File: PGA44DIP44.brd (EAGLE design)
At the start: 58.4 x 20.3 mm, 6 parts

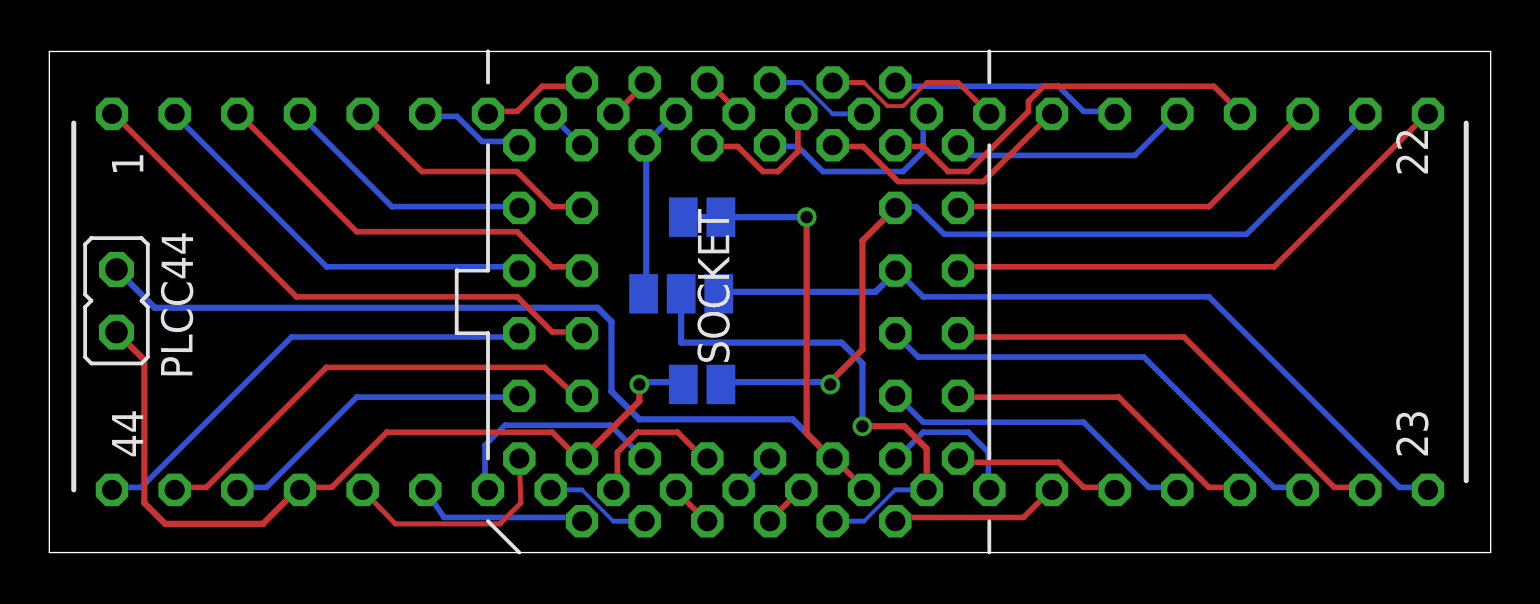
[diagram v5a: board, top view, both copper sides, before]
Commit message: * Fatal misassignment fixed for PGA44. * Update to EAGLE 8.1.0
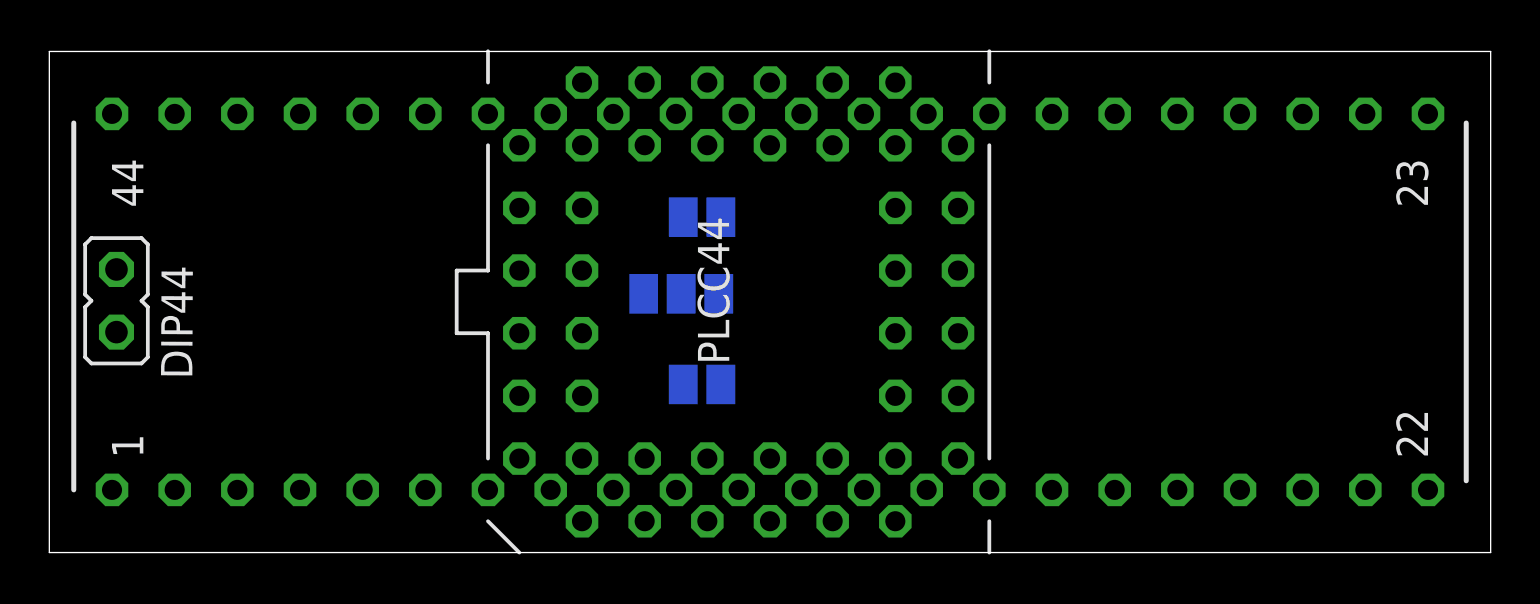
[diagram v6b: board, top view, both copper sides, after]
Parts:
- removed SOCKET: (no value), PGA44DIP44:PGA44
- added DIP44: DIP44, PGA44DIP44:DIP44
- PLCC44: value DIP44 -> PGA44; device PGA44DIP44:DIP44 -> PGA44DIP44:PGA44
- moved PLCC44 1.80 mm to (27.9, 10.2), turned to 90 degrees
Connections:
- net L1: now also DIP44.1; no longer SOCKET.1
- net L10: now also DIP44.10; no longer SOCKET.10
- net L11: now also DIP44.11; no longer SOCKET.11
- net L12: now also DIP44.12; no longer SOCKET.12
- net L13: now also DIP44.13; no longer SOCKET.13
- net L14: now also DIP44.14; no longer SOCKET.14
- net L15: now also DIP44.15; no longer SOCKET.15
- net L16: now also DIP44.16; no longer SOCKET.16
- net L17: now also DIP44.17; no longer SOCKET.17
- net L18: now also DIP44.18; no longer SOCKET.18
- net L19: now also DIP44.19; no longer SOCKET.19
- net L2: now also DIP44.2; no longer SOCKET.2
- net L20: now also DIP44.20; no longer SOCKET.20
- net L21: now also DIP44.21; no longer SOCKET.21
- net L22: now also DIP44.22; no longer SOCKET.22
- net L23: now also DIP44.23; no longer SOCKET.23
- net L24: now also DIP44.24; no longer SOCKET.24
- net L25: now also DIP44.25; no longer SOCKET.25
- net L26: now also DIP44.26; no longer SOCKET.26
- net L27: now also DIP44.27; no longer SOCKET.27
- net L28: now also DIP44.28; no longer SOCKET.28
- net L29: now also DIP44.29; no longer SOCKET.29
- net L3: now also DIP44.3; no longer SOCKET.3
- net L30: now also DIP44.30; no longer SOCKET.30
- net L31: now also DIP44.31; no longer SOCKET.31
- net L32: now also DIP44.32; no longer SOCKET.32
- net L33: now also DIP44.33; no longer SOCKET.33
- net L34: now also DIP44.34; no longer SOCKET.34
- net L35: now also DIP44.35; no longer SOCKET.35
- net L36: now also DIP44.36; no longer SOCKET.36
- net L37: now also DIP44.37; no longer SOCKET.37
- net L38: now also DIP44.38; no longer SOCKET.38
- net L39: now also DIP44.39; no longer SOCKET.39
- net L4: now also DIP44.4; no longer SOCKET.4
- net L40: now also DIP44.40; no longer SOCKET.40
- net L41: now also DIP44.41; no longer SOCKET.41
- net L42: now also DIP44.42; no longer SOCKET.42
- net L43: now also DIP44.43; no longer SOCKET.43
- net L44: now also DIP44.44; no longer SOCKET.44
- net L5: now also DIP44.5; no longer SOCKET.5
- net L6: now also DIP44.6; no longer SOCKET.6
- net L7: now also DIP44.7; no longer SOCKET.7
- net L8: now also DIP44.8; no longer SOCKET.8
- net L9: now also DIP44.9; no longer SOCKET.9
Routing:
- net L32: track 51.3 -> 0.00 mm, vias 1 -> 0
- net L21: track 34.4 -> 0.00 mm, vias 1 -> 0
- net L41: track 33.5 -> 0.00 mm, vias 1 -> 0
- net L23: track 32.8 -> 0.00 mm
- net L1: track 22.7 -> 0.00 mm
- net L22: track 21.7 -> 0.00 mm
- net L31: track 21.3 -> 0.00 mm, vias 1 -> 0
- net L24: track 19.2 -> 0.00 mm
- net L44: track 19.2 -> 0.00 mm
- net L25: track 19.1 -> 0.00 mm
- net L43: track 19.1 -> 0.00 mm
- net L2: track 16.6 -> 0.00 mm
- net L3: track 16.6 -> 0.00 mm
- net L19: track 16.6 -> 0.00 mm
- net L20: track 15.6 -> 0.00 mm
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
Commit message: Fixed artworks.
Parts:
- removed 　: (no value), PGA44DIP44:JP1
- removed 　　: (no value), PGA44DIP44:SJ
- removed 　　　: (no value), PGA44DIP44:SJ_2
- removed 　　　　: (no value), PGA44DIP44:SJ
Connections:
- net L10: no longer 　　　.3
- net L21: no longer 　　.2
- net L23: no longer 　　　.1
- net L31: no longer 　　　.2
- net L32: no longer 　.1, 　　　　.1, 　　　　.2
- net L41: no longer 　.2, 　　.1
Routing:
- net L23: track 0.00 -> 25.3 mm
- net L1: track 0.00 -> 22.7 mm
- net L22: track 0.00 -> 21.8 mm
- net L21: track 0.00 -> 21.6 mm
- net L24: track 0.00 -> 19.1 mm
- net L25: track 0.00 -> 19.1 mm
- net L44: track 0.00 -> 19.1 mm
- net L43: track 0.00 -> 19.1 mm
- net L3: track 0.00 -> 16.6 mm
- net L2: track 0.00 -> 16.6 mm
- net L20: track 0.00 -> 15.7 mm
- net L19: track 0.00 -> 15.3 mm
- net L16: track 0.00 -> 13.5 mm, vias 0 -> 1
- net L26: track 0.00 -> 13.0 mm
- net L27: track 0.00 -> 13.0 mm
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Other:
- board text added: "CC BY-NC-SA"
- board text added: "PC V1.1"
- board text added: "PGA44DIP44"

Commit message: Artwork predesigning (WIP)
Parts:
- added C1, C2, C3, C4: 0.1uF, rcl:C050-024X044
- added CN1: JTAG, con-lsta:FE05-1
- added IC1: LM2937ET-3.3/NOPB, PGA44DIP44:T03B
- added JP1: (no value), PGA44DIP44:JP1
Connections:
- new net GND: C1.2, C2.2, C3.2, C4.2, CN1.5, IC1.2
- new net N$1: IC1.3, JP1.1
- new net VCCINT: C3.1, C4.1, JP1.2
- new net VCCIO: C1.1, C2.1, IC1.1
- net L15: now also CN1.4
- net L16: now also CN1.1
- net L17: now also CN1.2
- net L30: now also CN1.3
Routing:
- net L30: track 6.07 -> 60.4 mm
- net VCCINT: track 0.00 -> 41.5 mm, vias 0 -> 3
- net L3: track 16.6 -> 41.1 mm
- net L17: track 9.42 -> 27.3 mm
- net VCCIO: track 0.00 -> 14.1 mm
- net L16: track 13.5 -> 27.1 mm
- net L15: track 7.61 -> 20.9 mm, vias 0 -> 2
- net L21: track 21.6 -> 33.2 mm
- net L19: track 15.3 -> 24.2 mm, vias 0 -> 3
- net L22: track 21.8 -> 30.2 mm, vias 0 -> 1
- net N$1: track 0.00 -> 4.58 mm
- net L13: track 4.34 -> 0.00 mm
- net L31: track 4.34 -> 0.00 mm
- net L37: track 4.34 -> 0.00 mm
- net L18: track 9.56 -> 10.9 mm
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- added copper zone on layer 1, net GND
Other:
- board text added: "GND"
- board text added: "TCK"
- board text added: "TDI"
- board text added: "TDO"
- board text added: "TMS"
- board text removed: "CC BY-NC-SA"
- board text removed: "PC V1.1"
- board text removed: "PGA44DIP44"
